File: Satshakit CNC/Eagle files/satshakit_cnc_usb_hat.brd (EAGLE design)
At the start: 57.2 x 46.5 mm, 30 parts

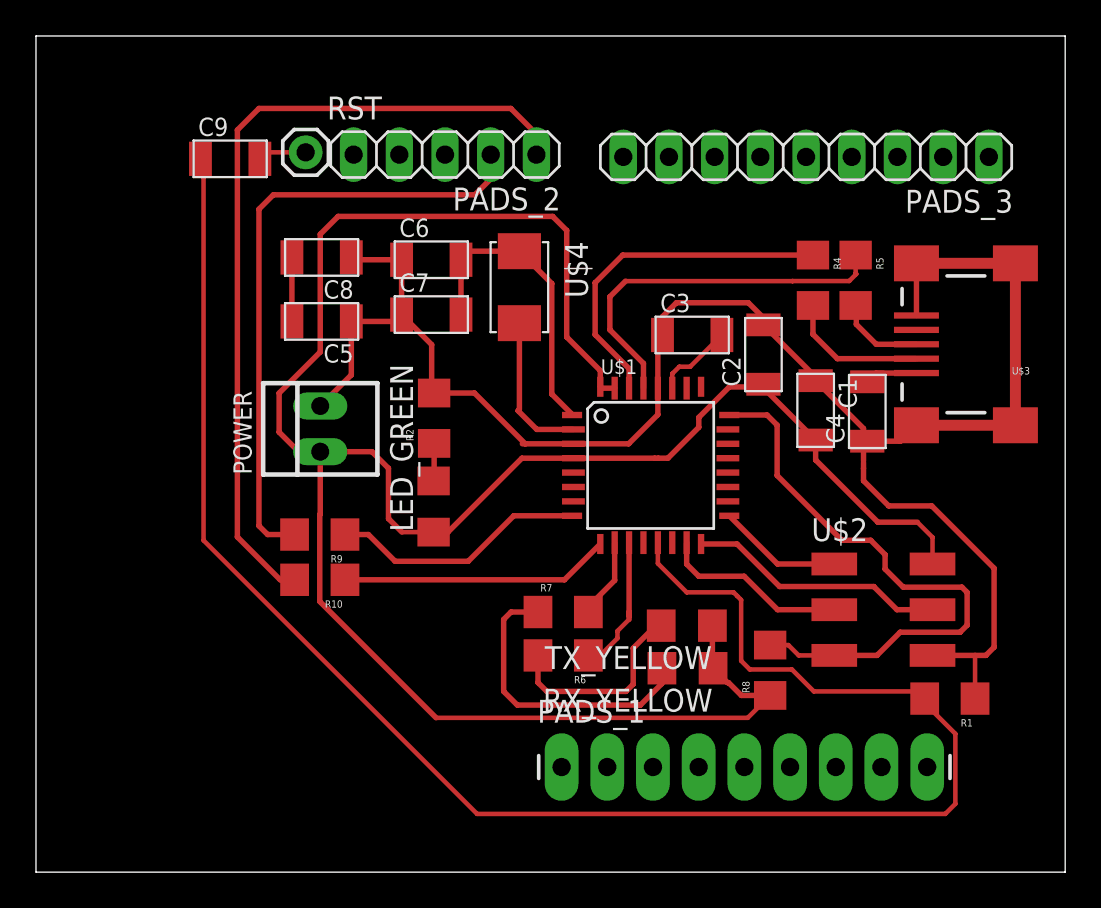
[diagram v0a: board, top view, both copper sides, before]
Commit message: New improved, simplified - yet to be properly testest - design. Most importantly it features a proper crystal trace and some elements redistribution
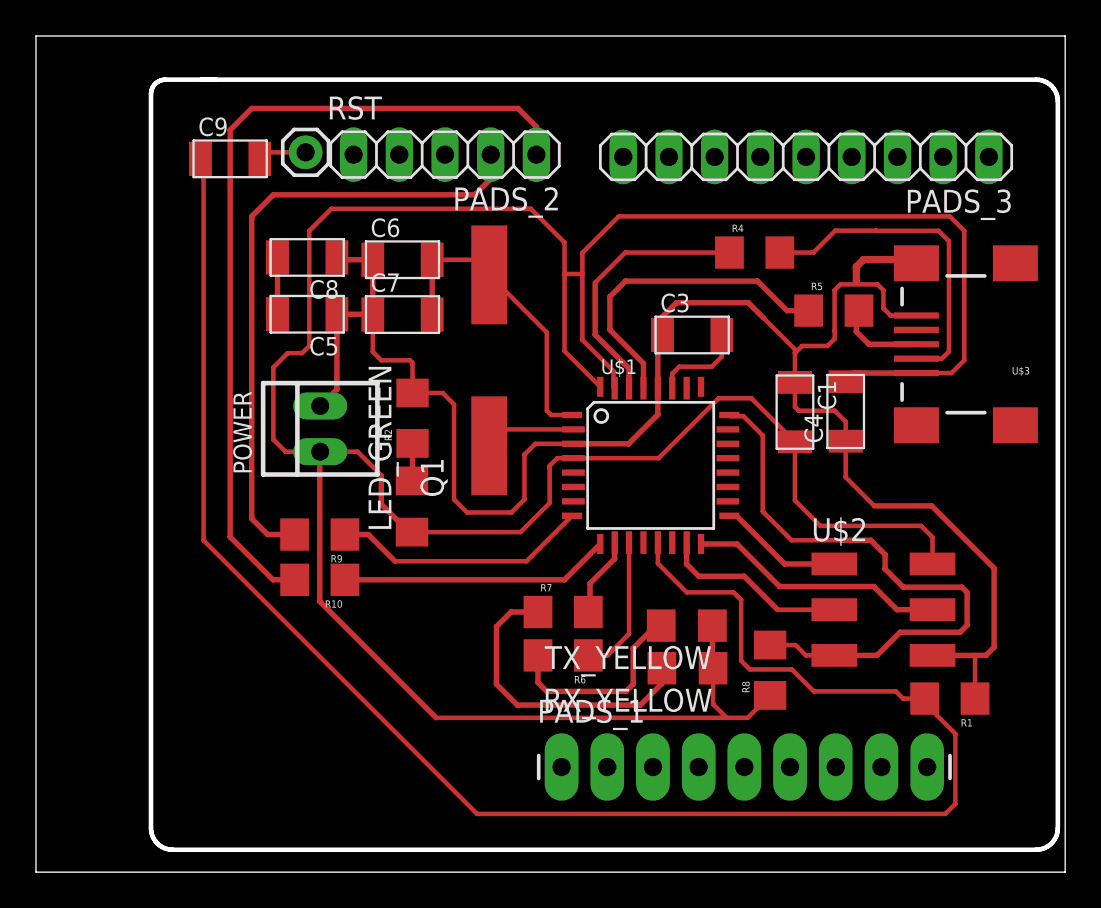
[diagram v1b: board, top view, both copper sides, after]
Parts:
- removed C2: 100nf, fab:C1206FAB
- removed U$4: 16Mhz, fab:2-SMD-5X3MM
- added Q1: 16Mhz, crystal:CSM-7X-DU
- moved R4 3.59 mm to (53.1, 30.0), turned to 0 degrees
- moved R5 2.08 mm to (57.5, 26.8), turned to 0 degrees
- moved C6 1.60 mm to (33.6, 29.6)
- moved C7 1.60 mm to (33.6, 26.5)
- moved C4 1.20 mm to (58.2, 21.2)
- moved LED_GREEN 1.20 mm to (34.1, 15.9)
- moved R2 1.20 mm to (34.1, 20.8)
- moved C1 1.15 mm to (55.4, 21.1)
- moved C5 0.89 mm to (28.3, 26.6)
- moved C8 0.80 mm to (28.3, 29.7)
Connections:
- removed net UVCC: C4.2, U$3.VBUS
- net GND: no longer C2.2, U$3.SHIELD@1, U$3.SHIELD@2, U$3.SHIELD@3, U$3.SHIELD@4
- net VCC: now also C4.2, U$3.VBUS; no longer C2.1
- net XTAL1: now also Q1.2; no longer U$4.P$1
- net XTAL2: now also Q1.1; no longer U$4.P$2
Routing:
- net VCC: track 129.2 -> 175.7 mm
- net N$4: track 7.91 -> 18.3 mm
- net GND: track 104.6 -> 97.7 mm
- net D-: track 19.4 -> 14.8 mm
- net N$12: track 0.00 -> 4.17 mm
- net D+: track 21.1 -> 17.9 mm
- net UVCC: track 2.93 -> 0.00 mm
- net XTAL2: track 8.41 -> 5.50 mm
- net SERIAL_TX: track 45.6 -> 46.7 mm
- net RST: track 33.5 -> 34.4 mm
- net N$6: track 4.45 -> 5.16 mm
- net SCK: track 10.9 -> 10.4 mm
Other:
- outline, holes or cut-outs redrawn

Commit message: Updated board. Reduced components and optimized traces. Added fancy writing
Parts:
- removed C5, C6: 10pf, fab:C1206FAB
- C7, C8: value 10pf -> 22 pf
- moved C7 5.09 mm to (30.0, 30.1)
- moved C8 4.25 mm to (30.1, 25.9), turned to 0 degrees
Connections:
- removed net N$3: C5.2, C8.2
- net GND: no longer C5.1, C6.1
- net XTAL1: no longer C6.2
- net XTAL2: now also C8.2
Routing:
- net XTAL2: track 5.50 -> 17.2 mm
- net N$28: track 0.00 -> 5.06 mm
- net N$19: track 0.00 -> 4.41 mm
- net GND: track 97.7 -> 93.3 mm
- net N$25: track 0.00 -> 4.33 mm
- net N$18: track 0.00 -> 4.33 mm
- net N$14: track 0.00 -> 4.33 mm
- net N$13: track 0.00 -> 4.26 mm
- net N$27: track 0.00 -> 4.26 mm
- net N$16: track 0.00 -> 4.26 mm
- net N$24: track 0.00 -> 4.00 mm
- net N$17: track 0.00 -> 4.00 mm
- net N$30: track 0.00 -> 3.53 mm
- net N$23: track 0.00 -> 2.78 mm
- net N$22: track 0.00 -> 2.78 mm
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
